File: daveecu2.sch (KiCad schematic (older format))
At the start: 6 parts, among them J1 CONN_BLACK, J2 CONN_GREY

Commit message: Update Schematic with a bunch of extra stuff
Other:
- note added: "unused"
- moved on the sheet: H1, H2, H3, H4, J1, J2

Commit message: Finish reroute again
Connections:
- net ST_SIG is gone; now on net GND: J1.B1
- net BOOST: now also J2.B8; no longer J2.C4
- net CAM: now also J2.A7; no longer J2.A2
- net CANH: now also J2.C6; no longer J2.B1
- net CANL: now also J2.C7; no longer J2.B2
- net CLT: now also J2.A5; no longer J2.A6
- net CLUTCH: now also J2.A2; no longer J2.A3
- net CRANK: now also J2.A8; no longer J2.A1
- net FAN: now also J2.C4; no longer J2.C2
- net FP: now also J2.C3; no longer J2.B3
- net GND: now also J1.A3, J1.A4, J1.A5, J1.A6, J2.C1, J2.C2; no longer J1.B5, J1.B6, J1.B7, J1.B8, J2.B4, J2.B7, J2.B8, J2.C5, J2.C6, J2.C7
- net IAT: now also J2.A4; no longer J2.A7
- net IDLE: now also J2.B7; no longer J2.C3
- net IGN-1: now also J1.C1; no longer J1.C2
- net IGN-2: now also J1.C2; no longer J1.C1
- net IGN-3: now also J1.C3; no longer J1.C4
- net IGN-4: now also J1.C4; no longer J1.C3
- net INJ-1: now also J1.C5; no longer J1.C6
- net INJ-2: now also J1.C6; no longer J1.C5
- net INJ-3: now also J1.C7; no longer J1.C8
- net INJ-4: now also J1.C8; no longer J1.C7
- net O2: now also J2.A6; no longer J2.A4
- net TACH: now also J2.C5; no longer J2.C1
- net TPS: now also J2.A3; no longer J2.A5
- net VBAT: now also J1.A8; no longer J1.A1
- net VPROT: now also J1.A7; no longer J1.A8
- new net A1: J1.B8
- new net A2: J1.B7
- new net A3: J1.B6
- new net A4: J1.B5
- new net AC: J2.A1
- new net HC1: J2.B4
- new net HC2: J2.B1
- new net HC3: J2.B2
- new net VVT: J2.B3

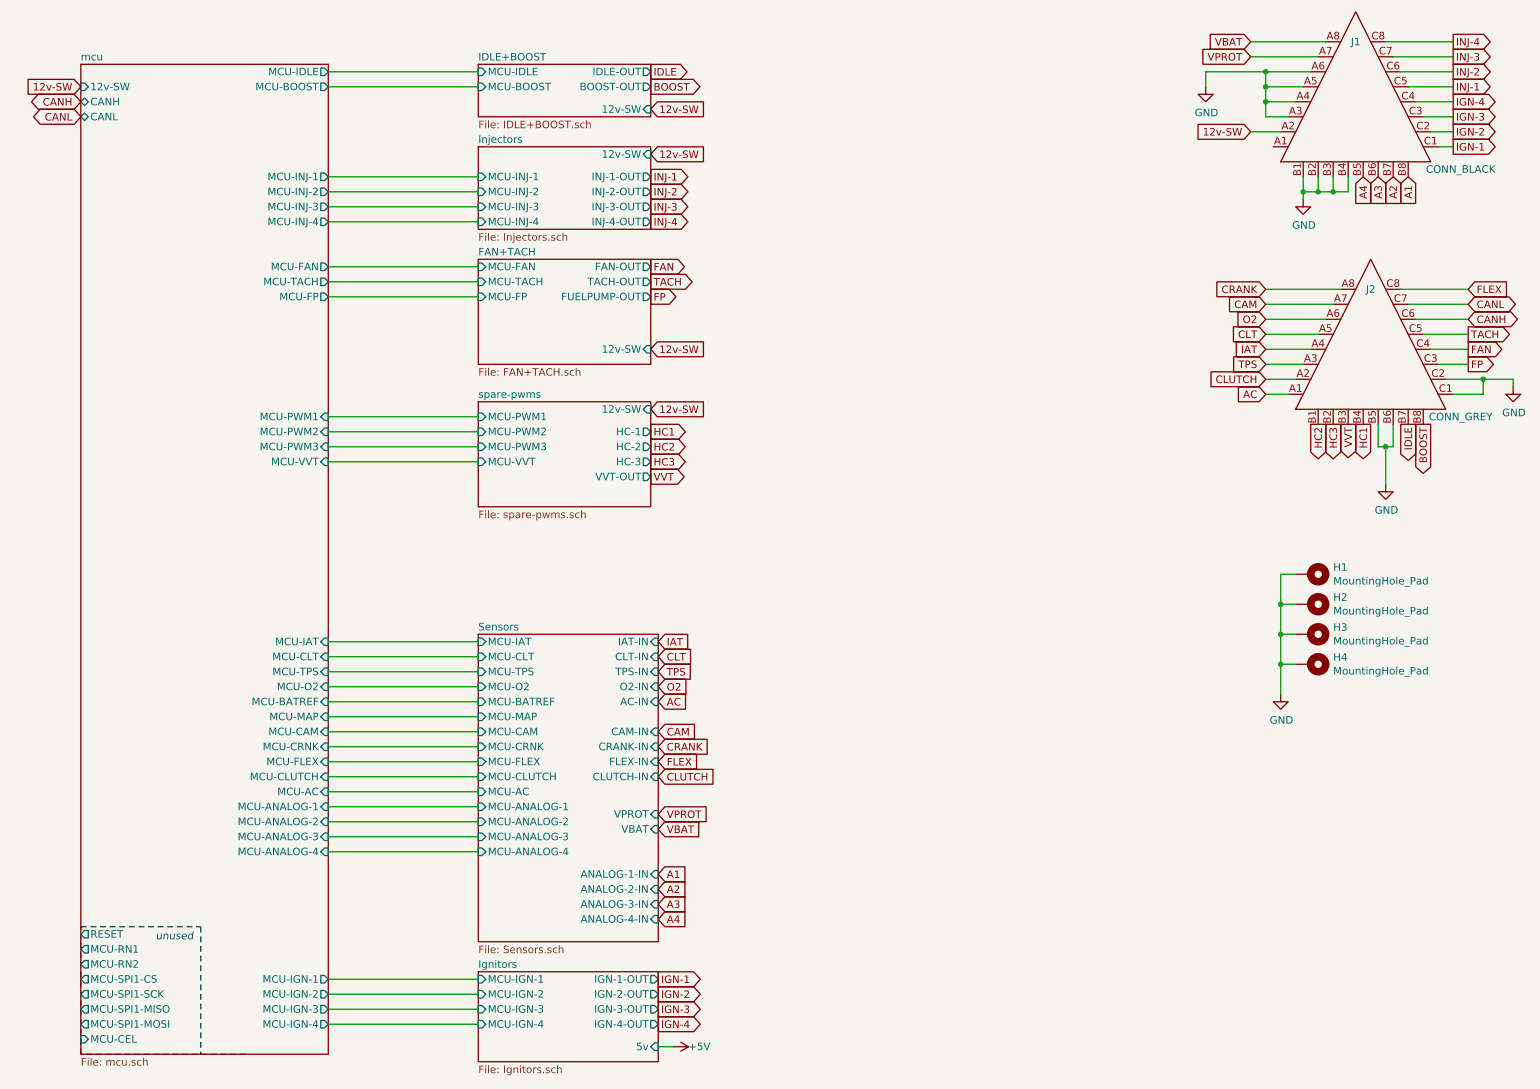
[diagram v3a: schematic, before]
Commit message: Schematic and Layout Updates
* cleanup unused pins for DRC
* swap swd connector for the fancy one the phill uses
* swap out the CAN transciever for one more suitable for 3v3
* reroute CAN differential pair
* clean up copper pours
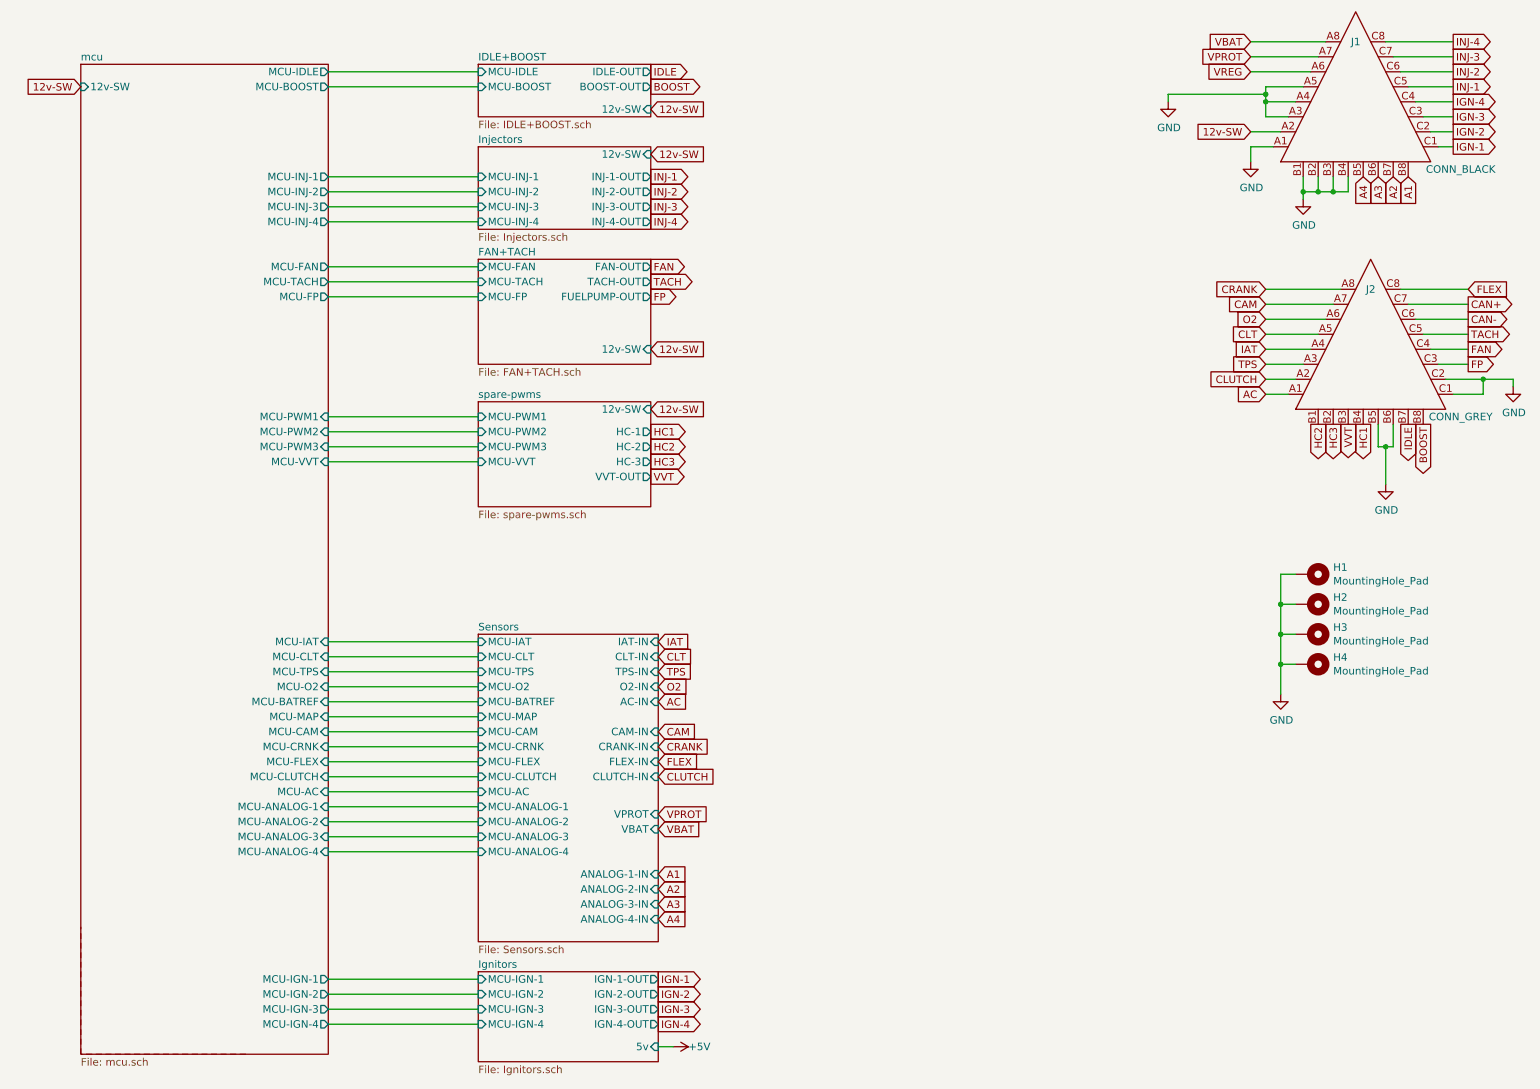
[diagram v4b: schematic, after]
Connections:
- net GND: now also J1.A1; no longer J1.A6
- net CANH renamed CAN-
- net CANL renamed CAN+
- new net VREG: J1.A6
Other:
- note removed: "unused"
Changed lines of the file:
@@
 Wire Wire Line
 	9400 5000 9400 4800
-Text GLabel 10650 2700 2    50   BiDi ~ 0
-CANH
-Text GLabel 10650 2600 2    50   BiDi ~ 0
-CANL
-Text GLabel 1400 1250 0    50   BiDi ~ 0
-CANH
-Text GLabel 1400 1350 0    50   BiDi ~ 0
-CANL
 Text GLabel 10650 2500 2    50   Input ~ 0
 FLEX
@@
 F8 "MCU-FAN" O R 3050 2350 50
 F9 "MCU-TACH" O R 3050 2450 50
-F10 "MCU-SPI1-SCK" O L 1400 7200 50
-F11 "MCU-SPI1-MISO" O L 1400 7300 50
-F12 "MCU-SPI1-MOSI" O L 1400 7400 50
-F13 "MCU-FP" O R 3050 2550 50
-F14 "MCU-IAT" I R 3050 4850 50
-F15 "MCU-CLT" I R 3050 4950 50
-F16 "MCU-TPS" I R 3050 5050 50
-F17 "MCU-O2" I R 3050 5150 50
-F18 "MCU-BATREF" I R 3050 5250 50
-F19 "MCU-MAP" I R 3050 5350 50
-F20 "MCU-CAM" I R 3050 5450 50
-F21 "MCU-CRNK" I R 3050 5550 50
-F22 "MCU-FLEX" I R 3050 5650 50
-F23 "MCU-CLUTCH" I R 3050 5750 50
-F24 "MCU-IGN-1" O R 3050 7100 50
-F25 "MCU-IGN-2" O R 3050 7200 50
-F26 "MCU-IGN-3" O R 3050 7300 50
-F27 "MCU-IGN-4" O R 3050 7400 50
-F28 "MCU-SPI1-CS" O L 1400 7100 50
-F29 "MCU-RN1" O L 1400 6900 50
-F30 "MCU-RN2" O L 1400 7000 50
-F31 "RESET" O L 1400 6800 50
-F32 "CANH" B L 1400 1250 50
-F33 "CANL" B L 1400 1350 50
-F34 "MCU-AC" I R 3050 5850 50
-F35 "MCU-CEL" I L 1400 7500 50
-F36 "MCU-VVT" I R 3050 3650 50
-F37 "MCU-PWM1" I R 3050 3350 50
-F38 "MCU-PWM2" I R 3050 3450 50
-F39 "MCU-PWM3" I R 3050 3550 50
-F40 "MCU-ANALOG-1" I R 3050 5950 50
-F41 "MCU-ANALOG-2" I R 3050 6050 50
-F42 "MCU-ANALOG-3" I R 3050 6150 50
-F43 "MCU-ANALOG-4" I R 3050 6250 50
-F44 "12v-SW" I L 1400 1150 50
+F10 "MCU-FP" O R 3050 2550 50
+F11 "MCU-IAT" I R 3050 4850 50
+F12 "MCU-CLT" I R 3050 4950 50
+F13 "MCU-TPS" I R 3050 5050 50
+F14 "MCU-O2" I R 3050 5150 50
+F15 "MCU-BATREF" I R 3050 5250 50
+F16 "MCU-MAP" I R 3050 5350 50
+F17 "MCU-CAM" I R 3050 5450 50
+F18 "MCU-CRNK" I R 3050 5550 50
+F19 "MCU-FLEX" I R 3050 5650 50
+F20 "MCU-CLUTCH" I R 3050 5750 50
+F21 "MCU-IGN-1" O R 3050 7100 50
+F22 "MCU-IGN-2" O R 3050 7200 50
+F23 "MCU-IGN-3" O R 3050 7300 50
+F24 "MCU-IGN-4" O R 3050 7400 50
+F25 "MCU-AC" I R 3050 5850 50
+F26 "MCU-VVT" I R 3050 3650 50
+F27 "MCU-PWM1" I R 3050 3350 50
+F28 "MCU-PWM2" I R 3050 3450 50
+F29 "MCU-PWM3" I R 3050 3550 50
+F30 "MCU-ANALOG-1" I R 3050 5950 50
+F31 "MCU-ANALOG-2" I R 3050 6050 50
+F32 "MCU-ANALOG-3" I R 3050 6150 50
+F33 "MCU-ANALOG-4" I R 3050 6250 50
+F34 "12v-SW" I L 1400 1150 50
 $EndSheet
 Text GLabel 5200 3300 2    50   Input ~ 0
@@
 Wire Notes Line
 	1400 7600 1400 6750
-Text Notes 1900 6850 0    50   Italic 0
-unused
-Wire Notes Line
-	1400 6750 2200 6750
-Wire Notes Line
-	2200 6750 2200 7600
 Text GLabel 5250 6400 2    50   Input ~ 0
 A1
@@
 L power:GND #PWR0109
 U 1 1 60BD53F4
-P 8900 1150
-F 0 "#PWR0109" H 8900 900 50  0001 C CNN
-F 1 "GND" H 8905 977 50  0000 C CNN
-F 2 "" H 8900 1150 50  0001 C CNN
-F 3 "" H 8900 1150 50  0001 C CNN
-	1    8900 1150
-	1    0    0    -1
-$EndComp
-Wire Wire Line
-	9600 1050 9300 1050
-Wire Wire Line
-	8900 1050 8900 1150
+P 8650 1250
+F 0 "#PWR0109" H 8650 1000 50  0001 C CNN
+F 1 "GND" H 8655 1077 50  0000 C CNN
+F 2 "" H 8650 1250 50  0001 C CNN
+F 3 "" H 8650 1250 50  0001 C CNN
+	1    8650 1250
+	1    0    0    -1
+$EndComp
 Wire Wire Line
 	9550 1150 9300 1150
 Wire Wire Line
-	9300 1150 9300 1050
-Connection ~ 9300 1050
-Wire Wire Line
-	9300 1050 8900 1050
-Wire Wire Line
 	9500 1250 9300 1250
 Wire Wire Line
-	9300 1250 9300 1150
-Connection ~ 9300 1150
+	9300 1250 9300 1200
 Wire Wire Line
 	9450 1350 9300 1350
@@
 	9300 1350 9300 1250
 Connection ~ 9300 1250
+Text GLabel 10650 2600 2    50   Output ~ 0
+CAN+
+Text GLabel 10650 2700 2    50   Output ~ 0
+CAN-
+Wire Wire Line
+	8650 1200 8650 1250
+Text GLabel 9200 1050 0    50   Input ~ 0
+VREG
+Wire Wire Line
+	9200 1050 9600 1050
+Wire Wire Line
+	8650 1200 9300 1200
+Connection ~ 9300 1200
+Wire Wire Line
+	9300 1200 9300 1150
+$Comp
+L power:GND #PWR0128
+U 1 1 6185B21E
+P 9200 1650
+F 0 "#PWR0128" H 9200 1400 50  0001 C CNN
+F 1 "GND" H 9205 1477 50  0000 C CNN
+F 2 "" H 9200 1650 50  0001 C CNN
+F 3 "" H 9200 1650 50  0001 C CNN
+	1    9200 1650
+	1    0    0    -1
+$EndComp
+Wire Wire Line
+	9200 1650 9200 1550
+Wire Wire Line
+	9200 1550 9350 1550
 $EndSCHEMATC
